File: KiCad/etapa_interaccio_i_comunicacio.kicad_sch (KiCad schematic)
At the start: 8 parts

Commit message: Alguns errors resolts, falten errors com canviar noms de unitats ''duplicats'', es fará en cas de que ja estigui tot bastant correcte
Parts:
- gave numbers to parts that had none: 8
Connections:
- net D0_control_bomba renamed DO_control_bomba
- net D0_control_tancament renamed DO_control_tancament
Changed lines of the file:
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@@
 		)
 	)
-	(global_label "D0_control_bomba"
+	(global_label "DO_control_bomba"
 		(shape input)
 		(at 175.26 85.09 180)
@@
 		)
 		(property "Intersheetrefs" "${INTERSHEET_REFS}"
-			(at 154.8581 85.09 0)
+			(at 154.7371 85.09 0)
 			(effects
 				(font
@@
 		)
 	)
-	(global_label "D0_control_tancament"
+	(global_label "DO_control_tancament"
 		(shape input)
 		(at 175.26 107.95 180)
@@
 		)
 		(property "Intersheetrefs" "${INTERSHEET_REFS}"
-			(at 151.2295 107.95 0)
+			(at 151.1085 107.95 0)
 			(effects
 				(font
@@
 		(dnp no)
 		(fields_autoplaced yes)
-		(property "Reference" "#PWR?"
+		(property "Reference" "#PWR0125"
 			(at 109.22 71.12 0)
 			(effects
@@
 			(project "PROJECTE_CASTRO_RIBAS"
 				(path "/27a7fca5-115a-450a-aa60-496c314f6c0e/2ae4c977-7e45-4d92-9ae0-450b29246e42"
-					(reference "#PWR?")
+					(reference "#PWR0125")
 					(unit 1)
 				)
@@
 		(dnp no)
 		(fields_autoplaced yes)
-		(property "Reference" "D?"
+		(property "Reference" "D1"
 			(at 202.2475 77.47 0)
 			(effects
@@
 			(project "PROJECTE_CASTRO_RIBAS"
 				(path "/27a7fca5-115a-450a-aa60-496c314f6c0e/2ae4c977-7e45-4d92-9ae0-450b29246e42"
-					(reference "D?")
+					(reference "D1")
 					(unit 1)
 				)
@@
 		(dnp no)
 		(fields_autoplaced yes)
-		(property "Reference" "#PWR?"
+		(property "Reference" "#PWR0127"
 			(at 86.36 93.98 0)
 			(effects
@@
 			(project "PROJECTE_CASTRO_RIBAS"
 				(path "/27a7fca5-115a-450a-aa60-496c314f6c0e/2ae4c977-7e45-4d92-9ae0-450b29246e42"
-					(reference "#PWR?")
+					(reference "#PWR0127")
 					(unit 1)
 				)
@@
 		(dnp no)
 		(fields_autoplaced yes)
-		(property "Reference" "SW?"
+		(property "Reference" "SW2"
 			(at 96.52 100.33 0)
 			(effects
@@
 			(project "PROJECTE_CASTRO_RIBAS"
 				(path "/27a7fca5-115a-450a-aa60-496c314f6c0e/2ae4c977-7e45-4d92-9ae0-450b29246e42"
-					(reference "SW?")
+					(reference "SW2")
 					(unit 1)
 				)
@@
 		(dnp no)
 		(fields_autoplaced yes)
-		(property "Reference" "R?"
+		(property "Reference" "R5"
 			(at 111.76 72.3899 0)
 			(effects
@@
 			(project "PROJECTE_CASTRO_RIBAS"
 				(path "/27a7fca5-115a-450a-aa60-496c314f6c0e/2ae4c977-7e45-4d92-9ae0-450b29246e42"
-					(reference "R?")
+					(reference "R5")
 					(unit 1)
 				)
@@
 		(dnp no)
 		(fields_autoplaced yes)
-		(property "Reference" "SW?"
+		(property "Reference" "SW1"
 			(at 96.52 77.47 0)
 			(effects
@@
 			(project "PROJECTE_CASTRO_RIBAS"
 				(path "/27a7fca5-115a-450a-aa60-496c314f6c0e/2ae4c977-7e45-4d92-9ae0-450b29246e42"
-					(reference "SW?")
+					(reference "SW1")
 					(unit 1)
 				)
@@
 		(dnp no)
 		(fields_autoplaced yes)
-		(property "Reference" "D?"
+		(property "Reference" "D2"
 			(at 202.2475 100.33 0)
 			(effects
@@
 			(project "PROJECTE_CASTRO_RIBAS"
 				(path "/27a7fca5-115a-450a-aa60-496c314f6c0e/2ae4c977-7e45-4d92-9ae0-450b29246e42"
-					(reference "D?")
+					(reference "D2")
 					(unit 1)
 				)
@@
 		(dnp no)
 		(fields_autoplaced yes)
-		(property "Reference" "#PWR?"
+		(property "Reference" "#PWR0122"
 			(at 208.28 92.71 0)
 			(effects
@@
 			(project "PROJECTE_CASTRO_RIBAS"
 				(path "/27a7fca5-115a-450a-aa60-496c314f6c0e/2ae4c977-7e45-4d92-9ae0-450b29246e42"
-					(reference "#PWR?")
+					(reference "#PWR0122")
 					(unit 1)
 				)
@@
 		(dnp no)
 		(fields_autoplaced yes)
-		(property "Reference" "#PWR?"
+		(property "Reference" "#PWR0123"
 			(at 208.28 116.84 0)
 			(effects
@@
 			(project "PROJECTE_CASTRO_RIBAS"
 				(path "/27a7fca5-115a-450a-aa60-496c314f6c0e/2ae4c977-7e45-4d92-9ae0-450b29246e42"
-					(reference "#PWR?")
+					(reference "#PWR0123")
 					(unit 1)
 				)
@@
 		(dnp no)
 		(fields_autoplaced yes)
-		(property "Reference" "R?"
+		(property "Reference" "R7"
 			(at 187.96 78.74 90)
 			(effects
@@
 			(project "PROJECTE_CASTRO_RIBAS"
 				(path "/27a7fca5-115a-450a-aa60-496c314f6c0e/2ae4c977-7e45-4d92-9ae0-450b29246e42"
-					(reference "R?")
+					(reference "R7")
 					(unit 1)
 				)
@@
 		(dnp no)
 		(fields_autoplaced yes)
-		(property "Reference" "R?"
+		(property "Reference" "R8"
 			(at 189.23 101.6 90)
 			(effects
@@
 			(project "PROJECTE_CASTRO_RIBAS"
 				(path "/27a7fca5-115a-450a-aa60-496c314f6c0e/2ae4c977-7e45-4d92-9ae0-450b29246e42"
-					(reference "R?")
+					(reference "R8")
 					(unit 1)
 				)
@@
 		(dnp no)
 		(fields_autoplaced yes)
-		(property "Reference" "#PWR?"
+		(property "Reference" "#PWR0126"
 			(at 86.36 116.84 0)
 			(effects
@@
 			(project "PROJECTE_CASTRO_RIBAS"
 				(path "/27a7fca5-115a-450a-aa60-496c314f6c0e/2ae4c977-7e45-4d92-9ae0-450b29246e42"
-					(reference "#PWR?")
+					(reference "#PWR0126")
 					(unit 1)
 				)
@@
 		(dnp no)
 		(fields_autoplaced yes)
-		(property "Reference" "R?"
+		(property "Reference" "R6"
 			(at 111.76 96.5199 0)
 			(effects
@@
 			(project "PROJECTE_CASTRO_RIBAS"
 				(path "/27a7fca5-115a-450a-aa60-496c314f6c0e/2ae4c977-7e45-4d92-9ae0-450b29246e42"
-					(reference "R?")
+					(reference "R6")
 					(unit 1)
 				)
@@
 		(on_board yes)
 		(dnp no)
-		(property "Reference" "#PWR?"
+		(property "Reference" "#PWR0124"
 			(at 109.22 95.25 0)
 			(effects
@@
 			(project "PROJECTE_CASTRO_RIBAS"
 				(path "/27a7fca5-115a-450a-aa60-496c314f6c0e/2ae4c977-7e45-4d92-9ae0-450b29246e42"
-					(reference "#PWR?")
-					(unit 1)
-				)
+					(reference "#PWR0124")
+					(unit 1)
+				)

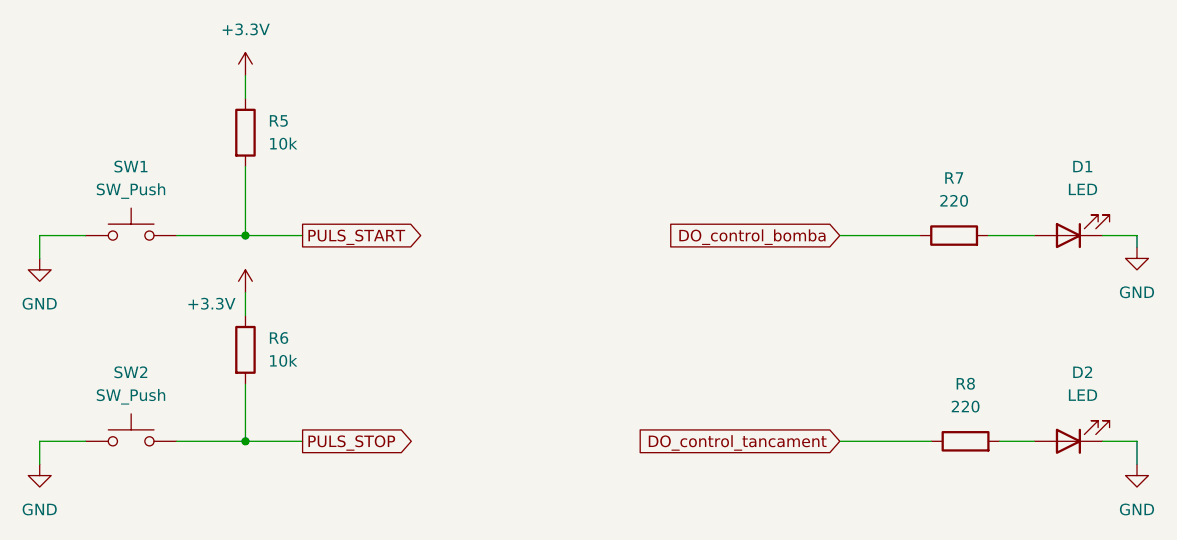
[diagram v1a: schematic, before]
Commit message: GNDs, VCCs col.locats correctament, pull-ups, etc ben connectats
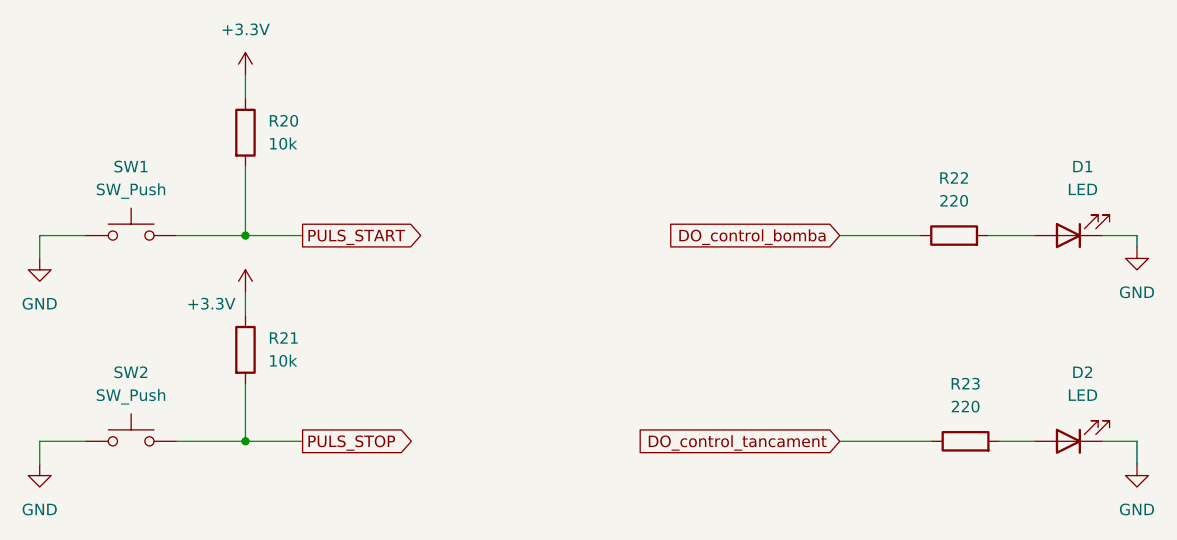
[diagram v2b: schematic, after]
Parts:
- renumbered R5 to R20, R6 to R21, R7 to R22, R8 to R23
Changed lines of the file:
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@@
 		(dnp no)
 		(fields_autoplaced yes)
-		(property "Reference" "R5"
+		(property "Reference" "R20"
 			(at 111.76 72.3899 0)
 			(effects
@@
 			(project "PROJECTE_CASTRO_RIBAS"
 				(path "/27a7fca5-115a-450a-aa60-496c314f6c0e/2ae4c977-7e45-4d92-9ae0-450b29246e42"
-					(reference "R5")
+					(reference "R20")
 					(unit 1)
 				)
@@
 		(dnp no)
 		(fields_autoplaced yes)
-		(property "Reference" "R7"
+		(property "Reference" "R22"
 			(at 187.96 78.74 90)
 			(effects
@@
 			(project "PROJECTE_CASTRO_RIBAS"
 				(path "/27a7fca5-115a-450a-aa60-496c314f6c0e/2ae4c977-7e45-4d92-9ae0-450b29246e42"
-					(reference "R7")
+					(reference "R22")
 					(unit 1)
 				)
@@
 		(dnp no)
 		(fields_autoplaced yes)
-		(property "Reference" "R8"
+		(property "Reference" "R23"
 			(at 189.23 101.6 90)
 			(effects
@@
 			(project "PROJECTE_CASTRO_RIBAS"
 				(path "/27a7fca5-115a-450a-aa60-496c314f6c0e/2ae4c977-7e45-4d92-9ae0-450b29246e42"
-					(reference "R8")
+					(reference "R23")
 					(unit 1)
 				)
@@
 		(dnp no)
 		(fields_autoplaced yes)
-		(property "Reference" "R6"
+		(property "Reference" "R21"
 			(at 111.76 96.5199 0)
 			(effects
@@
 			(project "PROJECTE_CASTRO_RIBAS"
 				(path "/27a7fca5-115a-450a-aa60-496c314f6c0e/2ae4c977-7e45-4d92-9ae0-450b29246e42"
-					(reference "R6")
-					(unit 1)
-				)
+					(reference "R21")
+					(unit 1)
+				)

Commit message: Afegides TOTES les petjades importants MENYS SENSOR de PRESSIO
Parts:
- SW1, SW2: footprint (none) -> Button_Switch_SMD:SW_DIP_SPSTx01_Slide_Copal_CHS-01B_W7.62mm_P1.27mm
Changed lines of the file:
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@@
 			)
 		)
-		(property "Footprint" ""
+		(property "Footprint" "Button_Switch_SMD:SW_DIP_SPSTx01_Slide_Copal_CHS-01B_W7.62mm_P1.27mm"
 			(at 96.52 102.87 0)
 			(effects
@@
 			)
 		)
-		(property "Footprint" ""
+		(property "Footprint" "Button_Switch_SMD:SW_DIP_SPSTx01_Slide_Copal_CHS-01B_W7.62mm_P1.27mm"
 			(at 96.52 80.01 0)
 			(effects

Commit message: Esquemàtic ACABAT
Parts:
- D1, D2: footprint (none) -> LED_THT:LED_D3.0mm
- R20, R21, R22, R23: footprint (none) -> Resistor_SMD:R_0805_2012Metric
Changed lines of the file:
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@@
 			)
 		)
-		(property "Footprint" ""
+		(property "Footprint" "LED_THT:LED_D3.0mm"
 			(at 200.66 85.09 0)
 			(effects
@@
 			)
 		)
-		(property "Footprint" ""
+		(property "Footprint" "Resistor_SMD:R_0805_2012Metric"
 			(at 107.442 73.66 90)
 			(effects
@@
 			)
 		)
-		(property "Footprint" ""
+		(property "Footprint" "LED_THT:LED_D3.0mm"
 			(at 200.66 107.95 0)
 			(effects
@@
 			)
 		)
-		(property "Footprint" ""
+		(property "Footprint" "Resistor_SMD:R_0805_2012Metric"
 			(at 187.96 86.868 90)
 			(effects
@@
 			)
 		)
-		(property "Footprint" ""
+		(property "Footprint" "Resistor_SMD:R_0805_2012Metric"
 			(at 189.23 109.728 90)
 			(effects
@@
 			)
 		)
-		(property "Footprint" ""
+		(property "Footprint" "Resistor_SMD:R_0805_2012Metric"
 			(at 107.442 97.79 90)
 			(effects
